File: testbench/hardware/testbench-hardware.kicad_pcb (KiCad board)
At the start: 2 copper layers, 88.9 x 88.9 mm, 40 parts, among them J1 ZIF DIP-16 Socket, Q1 ZTX458, SW1 Action, SW2 Mode Select, SW3 Enable Power

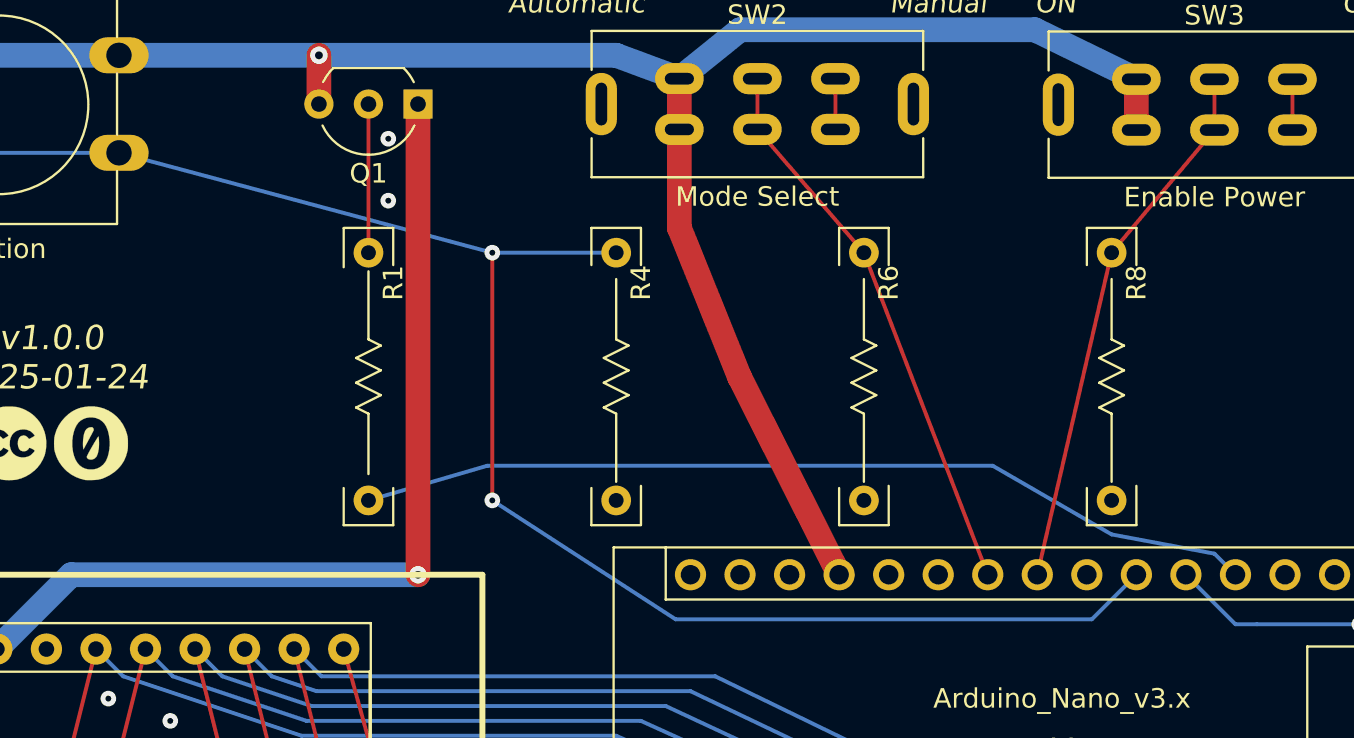
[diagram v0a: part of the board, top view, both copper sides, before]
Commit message: [testbench][hardware] change position of R1, R4, R6, R8 for nicer traces
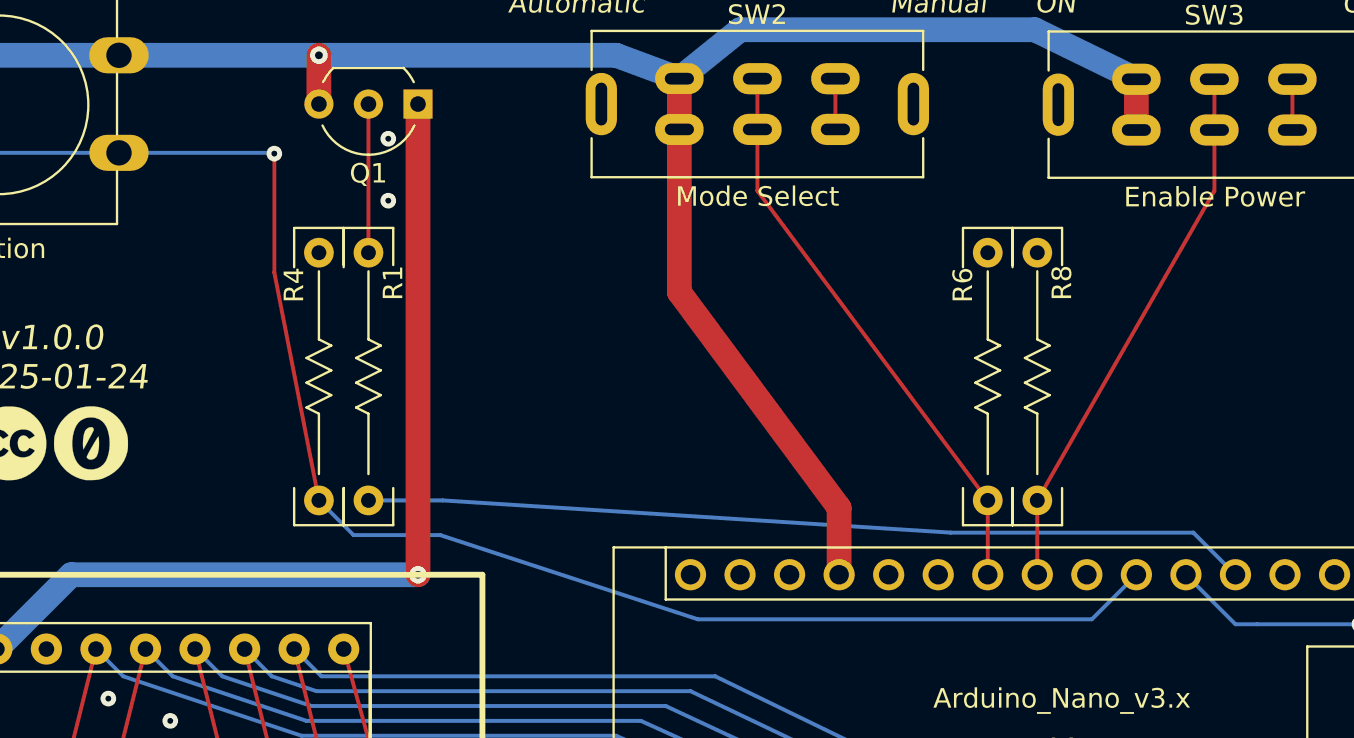
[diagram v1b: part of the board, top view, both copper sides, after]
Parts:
- moved R4 15.2 mm to (92.7, 90.2), turned to -90 degrees
- moved R6 6.35 mm to (127.0, 90.2), turned to -90 degrees
- moved R8 3.81 mm to (129.5, 90.2), turned to -90 degrees
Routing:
- net /ACTION_BUTTON: track 87.1 -> 82.8 mm, vias 2 -> 1
- net +5V: track 98.7 -> 99.6 mm
- net Net-(A1-A0): track 46.2 -> 45.4 mm
- net /MODE_SWITCH: track 28.6 -> 29.3 mm
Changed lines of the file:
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@@
   )
   (footprint "commons-passives_THT:Passive_THT_resistor_W2.54mm_L12.70mm" (layer "F.Cu")
-    (at 120.65 90.17 90)
+    (at 127 90.17 -90)
     (descr "THT resistor, width 100mils, lead vias 500mils apart")
     (tags "axial resistor tht")
@@
     (property "ki_keywords" "r resistor")
     (attr through_hole)
-    (fp_text reference "R6" (at 5.715 1.27 90) (layer "F.SilkS")
+    (fp_text reference "R6" (at -5.604 1.27 90) (layer "F.SilkS")
         (effects (font (size 1 1) (thickness 0.15)) (justify right))
     )
@@
     (fp_line (start 7.62 1.27) (end 5.715 1.27)
       (stroke (width 0.12) (type solid)) (layer "F.SilkS"))
-    (pad "1" thru_hole circle (at -6.35 0 90) (size 1.524 1.524) (drill 0.762) (layers "*.Cu" "*.Mask")
+    (pad "1" thru_hole circle (at -6.35 0 270) (size 1.524 1.524) (drill 0.762) (layers "*.Cu" "*.Mask")
       (net 4 "GND") (pintype "passive"))
-    (pad "2" thru_hole circle (at 6.35 0 90) (size 1.524 1.524) (drill 0.762) (layers "*.Cu" "*.Mask")
+    (pad "2" thru_hole circle (at 6.35 0 270) (size 1.524 1.524) (drill 0.762) (layers "*.Cu" "*.Mask")
       (net 23 "/MODE_SWITCH") (pintype "passive"))
     (model "${KISYS3DMOD}/Resistor_THT.3dshapes/R_Axial_DIN0207_L6.3mm_D2.5mm_P15.24mm_Horizontal.wrl"
@@
   )
   (footprint "commons-passives_THT:Passive_THT_resistor_W2.54mm_L12.70mm" (layer "F.Cu")
-    (at 133.35 90.17 90)
+    (at 129.54 90.17 -90)
     (descr "THT resistor, width 100mils, lead vias 500mils apart")
     (tags "axial resistor tht")
@@
     (property "ki_keywords" "r resistor")
     (attr through_hole)
-    (fp_text reference "R8" (at 5.715 1.27 90) (layer "F.SilkS")
+    (fp_text reference "R8" (at -5.715 -1.27 90) (layer "F.SilkS")
         (effects (font (size 1 1) (thickness 0.15)) (justify right))
     )
@@
     (fp_line (start 7.62 1.27) (end 5.715 1.27)
       (stroke (width 0.12) (type solid)) (layer "F.SilkS"))
-    (pad "1" thru_hole circle (at -6.35 0 90) (size 1.524 1.524) (drill 0.762) (layers "*.Cu" "*.Mask")
+    (pad "1" thru_hole circle (at -6.35 0 270) (size 1.524 1.524) (drill 0.762) (layers "*.Cu" "*.Mask")
       (net 4 "GND") (pintype "passive"))
-    (pad "2" thru_hole circle (at 6.35 0 90) (size 1.524 1.524) (drill 0.762) (layers "*.Cu" "*.Mask")
+    (pad "2" thru_hole circle (at 6.35 0 270) (size 1.524 1.524) (drill 0.762) (layers "*.Cu" "*.Mask")
       (net 21 "/POWER_ENABLE_SWITCH") (pintype "passive"))
     (model "${KISYS3DMOD}/Resistor_THT.3dshapes/R_Axial_DIN0207_L6.3mm_D2.5mm_P15.24mm_Horizontal.wrl"
@@
   )
   (footprint "commons-passives_THT:Passive_THT_resistor_W2.54mm_L12.70mm" (layer "F.Cu")
-    (at 107.95 90.17 90)
+    (at 92.71 90.17 -90)
     (descr "THT resistor, width 100mils, lead vias 500mils apart")
     (tags "axial resistor tht")
@@
     (property "ki_keywords" "r resistor")
     (attr through_hole)
-    (fp_text reference "R4" (at 5.715 1.27 270) (layer "F.SilkS")
+    (fp_text reference "R4" (at -5.604 1.27 -90) (layer "F.SilkS")
         (effects (font (size 1 1) (thickness 0.15)) (justify right))
     )
@@
     (fp_line (start 7.62 1.27) (end 5.715 1.27)
       (stroke (width 0.12) (type solid)) (layer "F.SilkS"))
-    (pad "1" thru_hole circle (at -6.35 0 90) (size 1.524 1.524) (drill 0.762) (layers "*.Cu" "*.Mask")
+    (pad "1" thru_hole circle (at -6.35 0 270) (size 1.524 1.524) (drill 0.762) (layers "*.Cu" "*.Mask")
       (net 4 "GND") (pintype "passive"))
-    (pad "2" thru_hole circle (at 6.35 0 90) (size 1.524 1.524) (drill 0.762) (layers "*.Cu" "*.Mask")
+    (pad "2" thru_hole circle (at 6.35 0 270) (size 1.524 1.524) (drill 0.762) (layers "*.Cu" "*.Mask")
       (net 20 "/ACTION_BUTTON") (pintype "passive"))
     (model "${KISYS3DMOD}/Resistor_THT.3dshapes/R_Axial_DIN0207_L6.3mm_D2.5mm_P15.24mm_Horizontal.wrl"
@@
   (segment (start 86.36 117.348) (end 89.408 117.348) (width 0.2) (layer "B.Cu") (net 15))
   (segment (start 89.408 117.348) (end 105.41 124.206) (width 0.2) (layer "B.Cu") (net 15))
-  (segment (start 138.6205 99.2505) (end 139.7 100.33) (width 0.2) (layer "B.Cu") (net 19))
-  (segment (start 133.35 98.263676) (end 138.6205 99.2505) (width 0.2) (layer "B.Cu") (net 19))
-  (segment (start 95.25 96.52) (end 101.346 94.742) (width 0.2) (layer "B.Cu") (net 19))
-  (segment (start 101.346 94.742) (end 127.254 94.742) (width 0.2) (layer "B.Cu") (net 19))
-  (segment (start 127.254 94.742) (end 133.35 98.263676) (width 0.2) (layer "B.Cu") (net 19))
-  (segment (start 101.6 83.82) (end 101.6 96.52) (width 0.2) (layer "F.Cu") (net 20))
-  (via (at 101.6 83.82) (size 0.8) (drill 0.3) (layers "F.Cu" "B.Cu") (net 20))
-  (via (at 101.6 96.52) (size 0.8) (drill 0.3) (layers "F.Cu" "B.Cu") (net 20))
+  (segment (start 99.06 96.52) (end 125.095 98.171) (width 0.2) (layer "B.Cu") (net 19))
+  (segment (start 137.541 98.171) (end 139.7 100.33) (width 0.2) (layer "B.Cu") (net 19))
+  (segment (start 95.25 96.52) (end 99.06 96.52) (width 0.2) (layer "B.Cu") (net 19))
+  (segment (start 125.095 98.171) (end 137.541 98.171) (width 0.2) (layer "B.Cu") (net 19))
+  (segment (start 90.424 84.836) (end 92.71 96.52) (width 0.2) (layer "F.Cu") (net 20))
+  (segment (start 90.424 84.836) (end 90.424 78.74) (width 0.2) (layer "F.Cu") (net 20))
+  (via (at 90.424 78.74) (size 0.8) (drill 0.3) (layers "F.Cu" "B.Cu") (net 20))
+  (segment (start 94.488 98.298) (end 98.933 98.298) (width 0.2) (layer "B.Cu") (net 20))
   (segment (start 134.62 100.33) (end 132.334 102.616) (width 0.2) (layer "B.Cu") (net 20))
-  (segment (start 101.6 96.52) (end 110.998 102.616) (width 0.2) (layer "B.Cu") (net 20))
+  (segment (start 90.424 78.74) (end 90.384 78.7) (width 0.2) (layer "B.Cu") (net 20))
   (segment (start 69.96 78.7) (end 82.46 78.7) (width 0.2) (layer "B.Cu") (net 20))
-  (segment (start 132.334 102.616) (end 110.998 102.616) (width 0.2) (layer "B.Cu") (net 20))
-  (segment (start 82.46 78.7) (end 101.6 83.82) (width 0.2) (layer "B.Cu") (net 20))
-  (segment (start 101.6 83.82) (end 107.95 83.82) (width 0.2) (layer "B.Cu") (net 20))
+  (segment (start 132.334 102.616) (end 112.141 102.616) (width 0.2) (layer "B.Cu") (net 20))
+  (segment (start 98.933 98.298) (end 112.141 102.616) (width 0.2) (layer "B.Cu") (net 20))
+  (segment (start 92.71 96.52) (end 94.488 98.298) (width 0.2) (layer "B.Cu") (net 20))
+  (segment (start 90.384 78.7) (end 82.46 78.7) (width 0.2) (layer "B.Cu") (net 20))
+  (segment (start 129.54 100.33) (end 129.54 96.52) (width 0.2) (layer "F.Cu") (net 21))
+  (segment (start 138.62 80.645) (end 129.54 96.52) (width 0.2) (layer "F.Cu") (net 21))
+  (segment (start 138.62 77.53) (end 138.62 80.645) (width 0.2) (layer "F.Cu") (net 21))
   (segment (start 138.62 74.93) (end 138.62 77.53) (width 0.2) (layer "F.Cu") (net 21))
-  (segment (start 129.54 100.33) (end 133.35 83.82) (width 0.2) (layer "F.Cu") (net 21))
-  (segment (start 133.35 83.82) (end 138.62 77.53) (width 0.2) (layer "F.Cu") (net 21))
-  (segment (start 127 100.33) (end 120.65 83.82) (width 0.2) (layer "F.Cu") (net 23))
   (segment (start 115.19 74.9) (end 115.19 77.5) (width 0.2) (layer "F.Cu") (net 23))
-  (segment (start 120.65 83.82) (end 115.19 77.5) (width 0.2) (layer "F.Cu") (net 23))
+  (segment (start 127 100.33) (end 127 96.52) (width 0.2) (layer "F.Cu") (net 23))
+  (segment (start 115.19 77.5) (end 115.19 80.645) (width 0.2) (layer "F.Cu") (net 23))
+  (segment (start 115.19 80.645) (end 127 96.52) (width 0.2) (layer "F.Cu") (net 23))
   (segment (start 88.9 111.76) (end 88.9 118.11) (width 0.2) (layer "F.Cu") (net 26))
   (segment (start 114.3 128.27) (end 114.3 118.872) (width 0.2) (layer "F.Cu") (net 26))
@@
   (segment (start 114.3 118.872) (end 128.27 118.872) (width 0.2) (layer "B.Cu") (net 26))
   (segment (start 113.03 127) (end 114.3 128.27) (width 0.2) (layer "B.Cu") (net 26))
-  (segment (start 111.19 77.5) (end 111.19 82.55) (width 1.27) (layer "F.Cu") (net 27))
+  (segment (start 119.38 100.33) (end 119.38 96.901) (width 1.27) (layer "F.Cu") (net 27))
+  (segment (start 111.19 77.5) (end 111.19 85.852) (width 1.27) (layer "F.Cu") (net 27))
   (segment (start 134.62 77.53) (end 134.62 74.93) (width 1.27) (layer "F.Cu") (net 27))
-  (segment (start 114.275388 90.194612) (end 111.19 82.55) (width 1.27) (layer "F.Cu") (net 27))
+  (segment (start 119.38 96.901) (end 111.19 85.852) (width 1.27) (layer "F.Cu") (net 27))
   (segment (start 111.19 74.9) (end 111.19 77.5) (width 1.27) (layer "F.Cu") (net 27))
   (segment (start 92.71 76.2) (end 92.71 73.7) (width 1.27) (layer "F.Cu") (net 27))
-  (segment (start 114.275388 90.194612) (end 119.38 100.33) (width 1.27) (layer "F.Cu") (net 27))
   (via (at 92.71 73.7) (size 0.9) (drill 0.4) (layers "F.Cu" "B.Cu") (net 27))
   (segment (start 129.413 72.39) (end 114.3 72.39) (width 1.27) (layer "B.Cu") (net 27))
